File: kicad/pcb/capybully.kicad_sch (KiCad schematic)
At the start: 15 parts, among them J1 SM04B-SRSS-TB(LF)(SN), U1 STM32F072CBT6

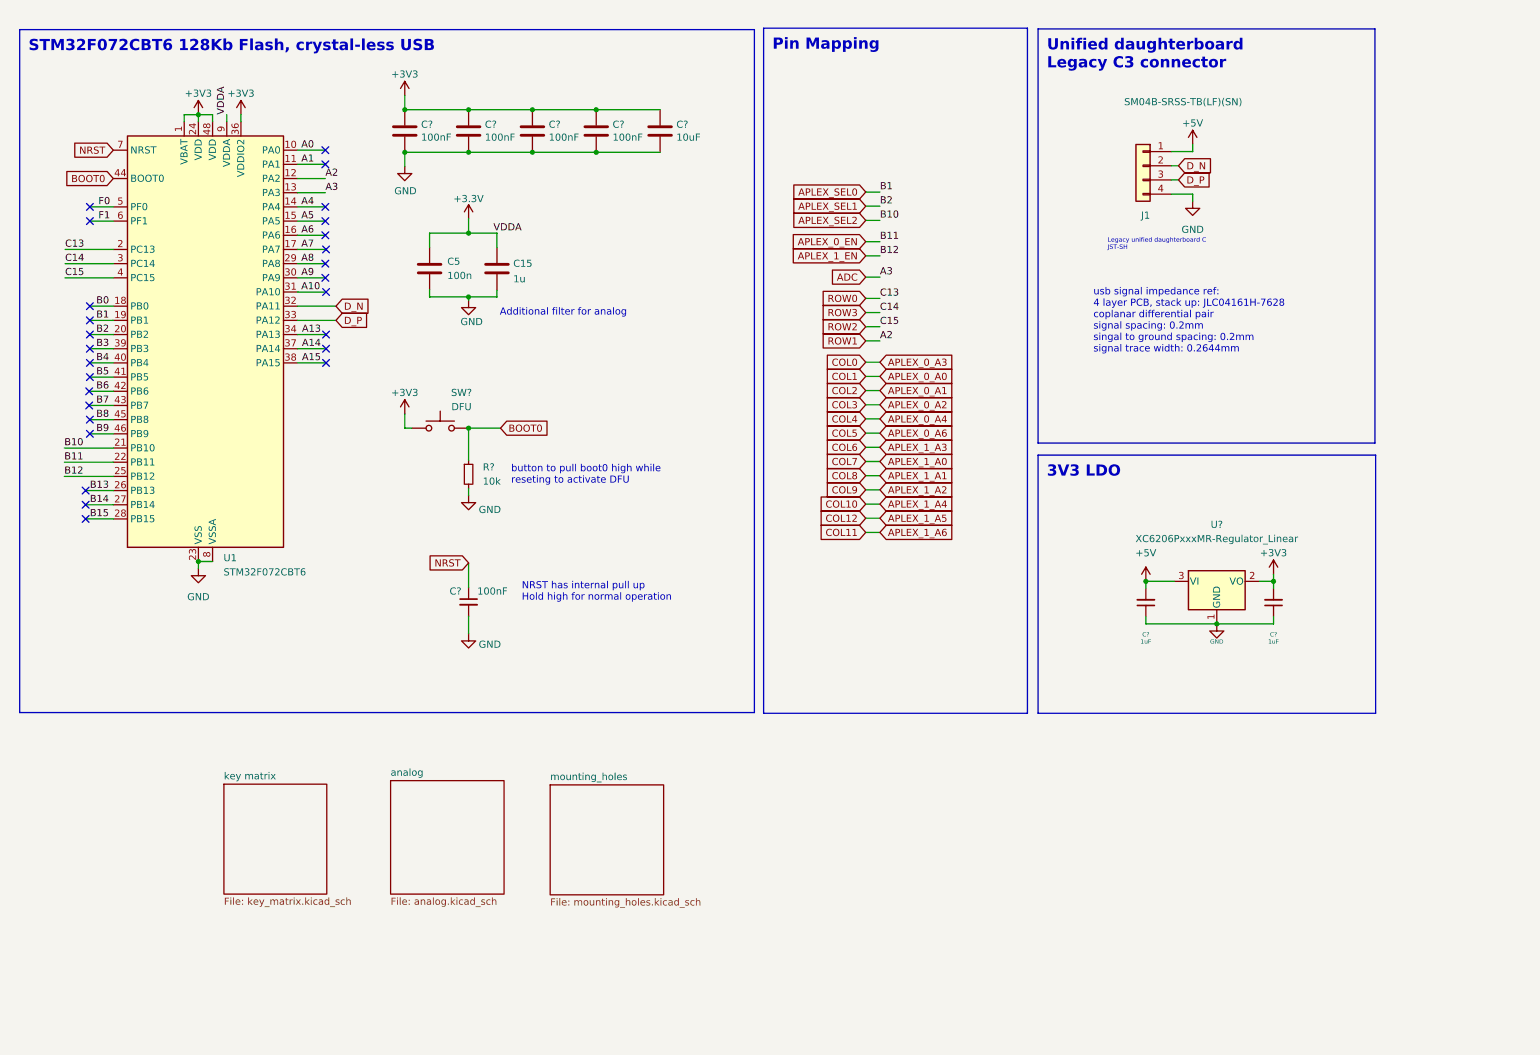
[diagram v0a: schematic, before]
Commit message: should be ok for proto order
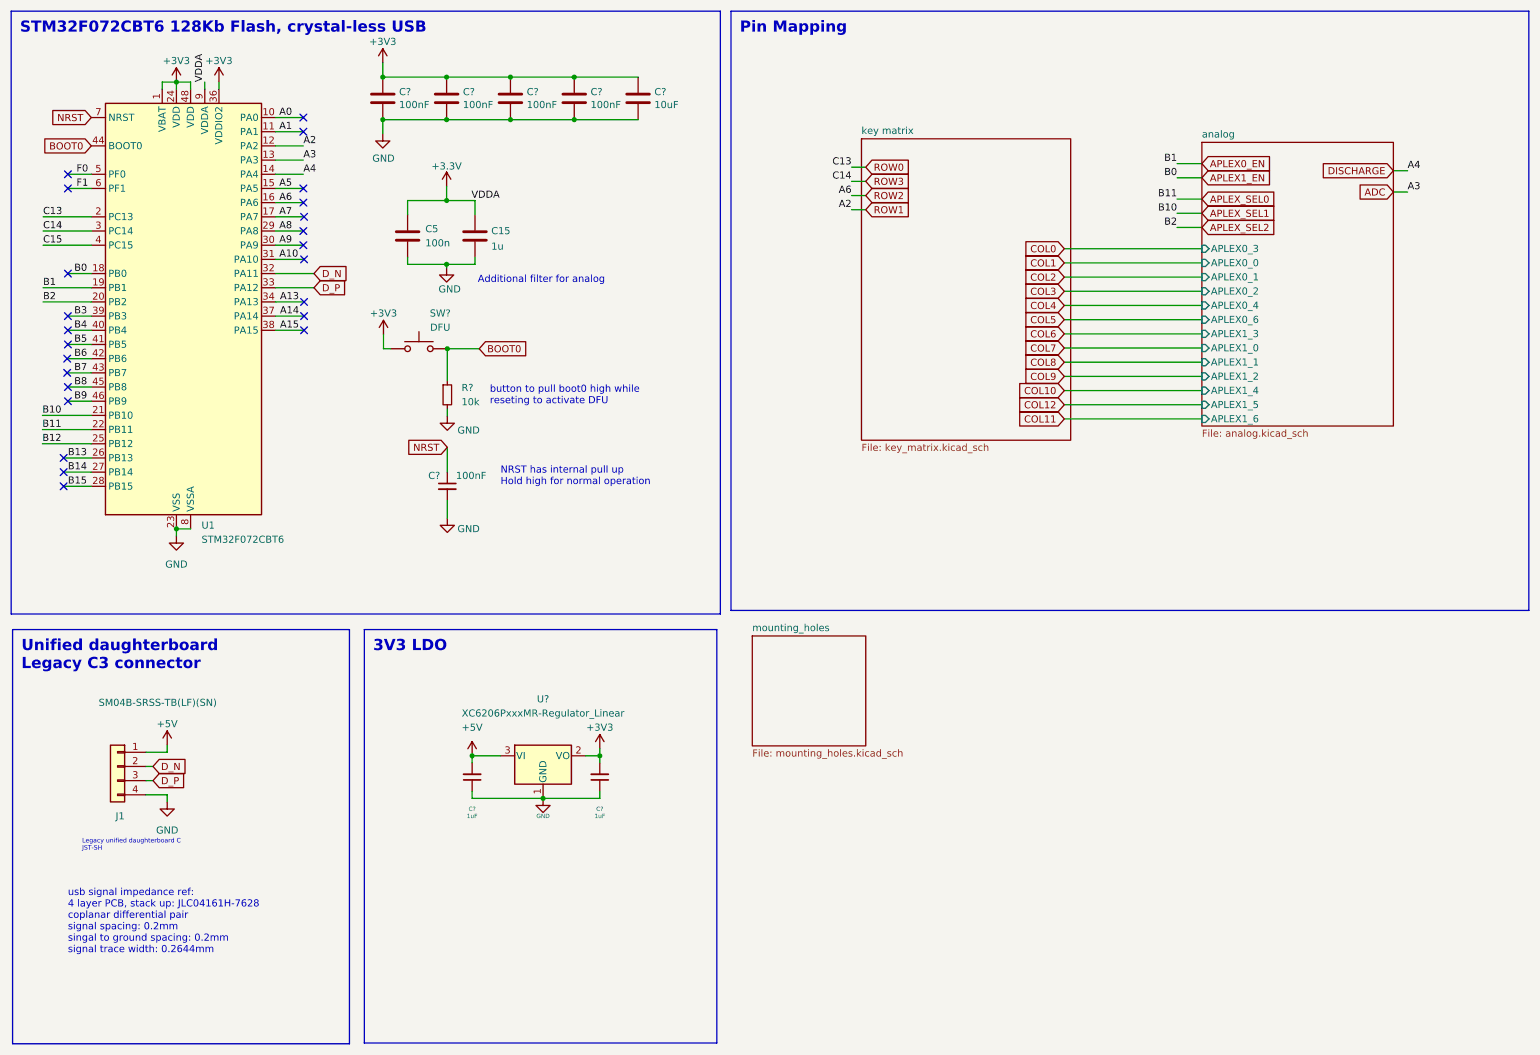
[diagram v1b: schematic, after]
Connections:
- net A6 is gone; now on net ROW2: U1.16 (PA6)
- net APLEX_0_EN is gone; now on net APLEX_SEL0: U1.22 (PB11)
- net APLEX_SEL0: no longer U1.19 (PB1)
- net APLEX_SEL1: now also U1.21 (PB10); no longer U1.20 (PB2)
- net APLEX_SEL2: now also U1.20 (PB2); no longer U1.21 (PB10)
- net ROW2: no longer U1.4 (PC15)
- net A4 renamed DISCHARGE
- net APLEX_1_EN renamed B12
- net B0 renamed APLEX1_EN
- new net APLEX0_EN: U1.19 (PB1)
- new net C15: U1.4 (PC15)
- no-connect marks 27 -> 24
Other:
- sheet analog ports: added APLEX0_0, APLEX0_1, APLEX0_2, APLEX0_3, APLEX0_4, APLEX0_6, APLEX1_0, APLEX1_1, APLEX1_2, APLEX1_3, APLEX1_4, APLEX1_5, APLEX1_6; removed none
- moved on the sheet: C15, C5, C?, J1, R?, SW?, U1, U?

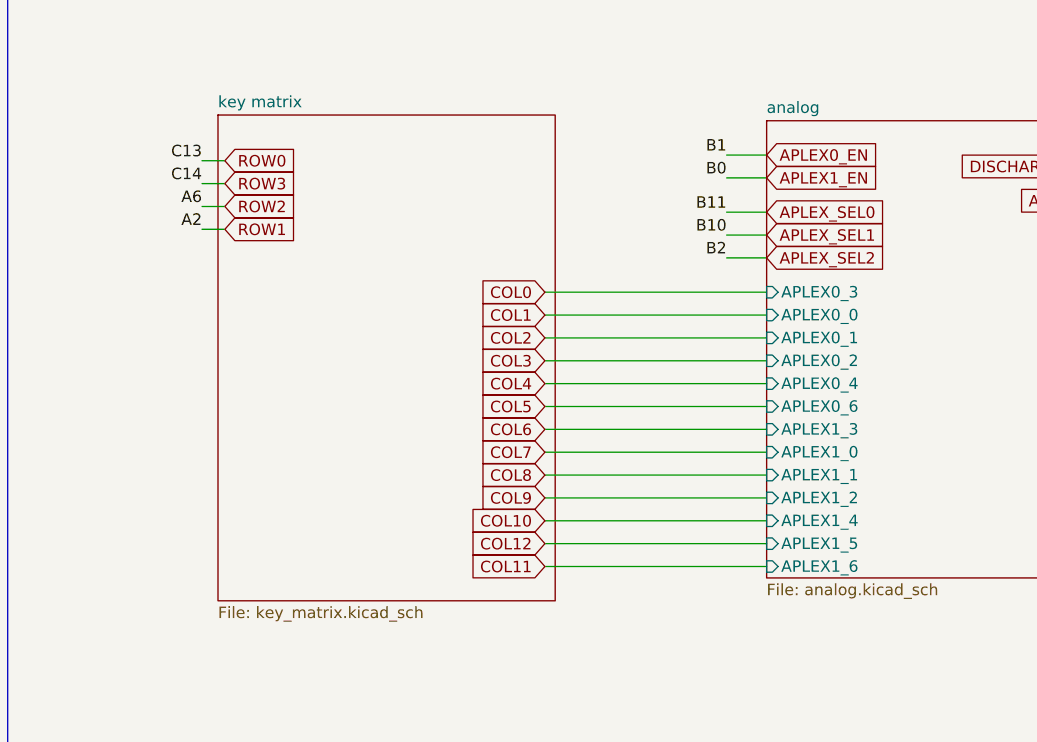
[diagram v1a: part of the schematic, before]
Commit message: adding right shift option
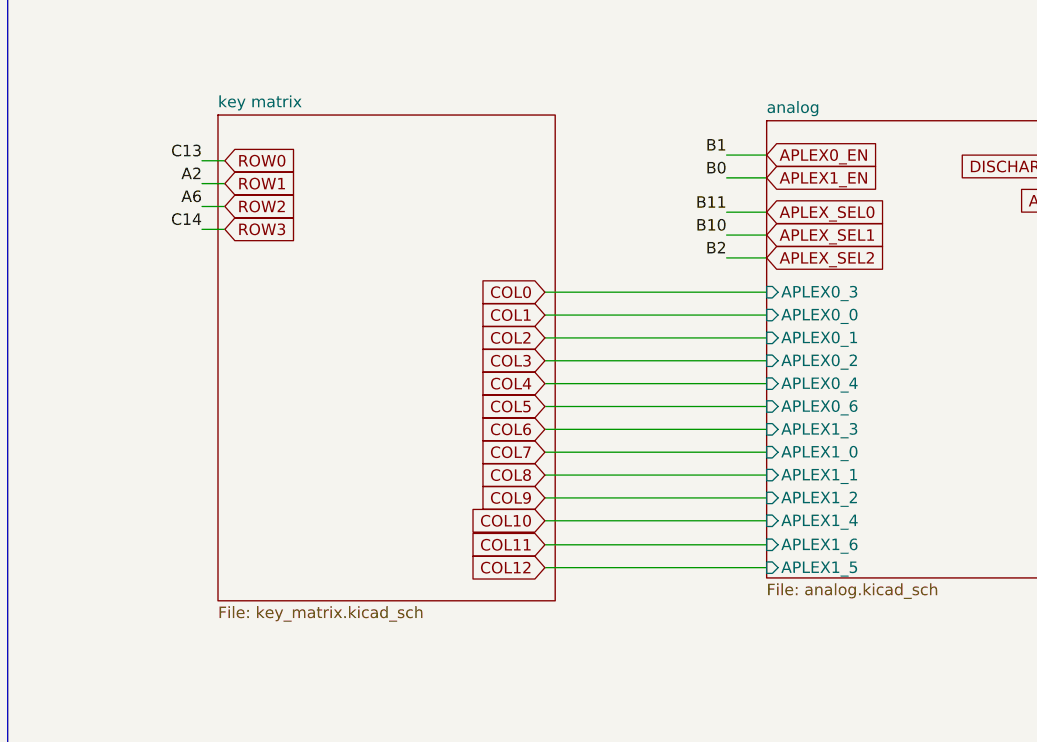
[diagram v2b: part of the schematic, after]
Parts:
- SW?: footprint Connector_PinHeader_2.00mm:PinHeader_1x02_P2.00mm_Vertical -> Connector_PinHeader_2.54mm:PinHeader_1x02_P2.54mm_Vertical
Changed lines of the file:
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@@
-    (stroke (width 0) (type default))
-  )
-  (wire (pts (xy 200.66 82.55) (xy 225.298 82.55))
     (stroke (width 0) (type default))
   )
@@
     (stroke (width 0) (type default))
   )
+  (wire (pts (xy 200.66 85.217) (xy 225.298 85.217))
+    (stroke (width 0) (type default))
+  )
   (wire (pts (xy 21.463 92.075) (xy 26.416 92.075))
     (stroke (width 0) (type default))
@@
     (stroke (width 0) (type default))
   )
-  (wire (pts (xy 200.66 85.09) (xy 225.298 85.09))
-    (stroke (width 0) (type default))
-  )
   (wire (pts (xy 17.78 61.595) (xy 26.416 61.595))
     (stroke (width 0) (type default))
@@
   )
   (wire (pts (xy 259.588 40.64) (xy 262.128 40.64))
+    (stroke (width 0) (type default))
+  )
+  (wire (pts (xy 200.66 82.677) (xy 225.298 82.677))
     (stroke (width 0) (type default))
   )
@@
     (stroke (width 0) (type solid))
   )
-  (wire (pts (xy 162.56 42.545) (xy 165.1 42.545))
+  (wire (pts (xy 162.56 47.625) (xy 165.1 47.625))
     (stroke (width 0) (type default))
   )
@@
     (stroke (width 0) (type default))
   )
-  (wire (pts (xy 162.56 47.625) (xy 165.1 47.625))
+  (wire (pts (xy 162.56 42.545) (xy 165.1 42.545))
     (stroke (width 0) (type default))
   )
@@
     (effects (font (size 1.27 1.27)) (justify left bottom))
   )
-  (label "C14" (at 162.56 42.545 180) (fields_autoplaced)
+  (label "C14" (at 162.56 47.625 180) (fields_autoplaced)
     (effects (font (size 1.27 1.27)) (justify right bottom))
   )
@@
     (effects (font (size 1.27 1.27)) (justify left bottom))
   )
-  (label "A2" (at 162.56 47.625 180) (fields_autoplaced)
+  (label "A2" (at 162.56 42.545 180) (fields_autoplaced)
     (effects (font (size 1.27 1.27)) (justify right bottom))
   )
@@
     )
   )
-  (global_label "COL11" (shape input) (at 200.66 85.09 180) (fields_autoplaced)
+  (global_label "COL11" (shape input) (at 200.66 82.677 180) (fields_autoplaced)
     (effects (font (size 1.27 1.27)) (justify right))
-    (property "Intersheetrefs" "${INTERSHEET_REFS}" (at 191.7066 85.09 0)
+    (property "Intersheetrefs" "${INTERSHEET_REFS}" (at 191.7066 82.677 0)
       (effects (font (size 1.27 1.27)) (justify right) hide)
     )
@@
     )
   )
-  (global_label "COL12" (shape input) (at 200.66 82.55 180) (fields_autoplaced)
+  (global_label "COL12" (shape input) (at 200.66 85.217 180) (fields_autoplaced)
     (effects (font (size 1.27 1.27)) (justify right))
-    (property "Intersheetrefs" "${INTERSHEET_REFS}" (at 191.7066 82.55 0)
+    (property "Intersheetrefs" "${INTERSHEET_REFS}" (at 191.7066 85.217 0)
       (effects (font (size 1.27 1.27)) (justify right) hide)
     )
@@
     )
   )
-  (global_label "ROW3" (shape input) (at 165.1 42.545 0) (fields_autoplaced)
+  (global_label "ROW3" (shape input) (at 165.1 47.625 0) (fields_autoplaced)
     (effects (font (size 1.27 1.27)) (justify left))
-    (property "Intersheetrefs" "${INTERSHEET_REFS}" (at 173.2672 42.545 0)
+    (property "Intersheetrefs" "${INTERSHEET_REFS}" (at 173.2672 47.625 0)
       (effects (font (size 1.27 1.27)) (justify left) hide)
     )
@@
     )
   )
-  (global_label "ROW1" (shape input) (at 165.1 47.625 0) (fields_autoplaced)
+  (global_label "ROW1" (shape input) (at 165.1 42.545 0) (fields_autoplaced)
     (effects (font (size 1.27 1.27)) (justify left))
-    (property "Intersheetrefs" "${INTERSHEET_REFS}" (at 173.2672 47.625 0)
+    (property "Intersheetrefs" "${INTERSHEET_REFS}" (at 173.2672 42.545 0)
       (effects (font (size 1.27 1.27)) (justify left) hide)
     )
@@
       (effects (font (size 1.27 1.27)))
     )
-    (property "Footprint" "Connector_PinHeader_2.00mm:PinHeader_1x02_P2.00mm_Vertical" (at 85.09 67.437 0)
+    (property "Footprint" "Connector_PinHeader_2.54mm:PinHeader_1x02_P2.54mm_Vertical" (at 85.09 67.437 0)
       (effects (font (size 1.27 1.27)) hide)
     )
@@
       (effects (font (size 1.27 1.27)) (justify left top))
     )
-    (pin "APLEX1_5" input (at 225.298 82.55 180)
+    (pin "APLEX1_5" input (at 225.298 85.217 180)
       (effects (font (size 1.27 1.27)) (justify left))
     )
@@
       (effects (font (size 1.27 1.27)) (justify left))
     )
-    (pin "APLEX1_6" input (at 225.298 85.09 180)
-      (effects (font (size 1.27 1.27)) (justify left))
-    )
+    (pin "APLEX1_6" input (at 225.298 82.677 180)
+      (effects (font (size 1.27 1.27)) (justify left))
+    )
